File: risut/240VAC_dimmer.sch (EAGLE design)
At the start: 11 parts, among them T1 TICP206

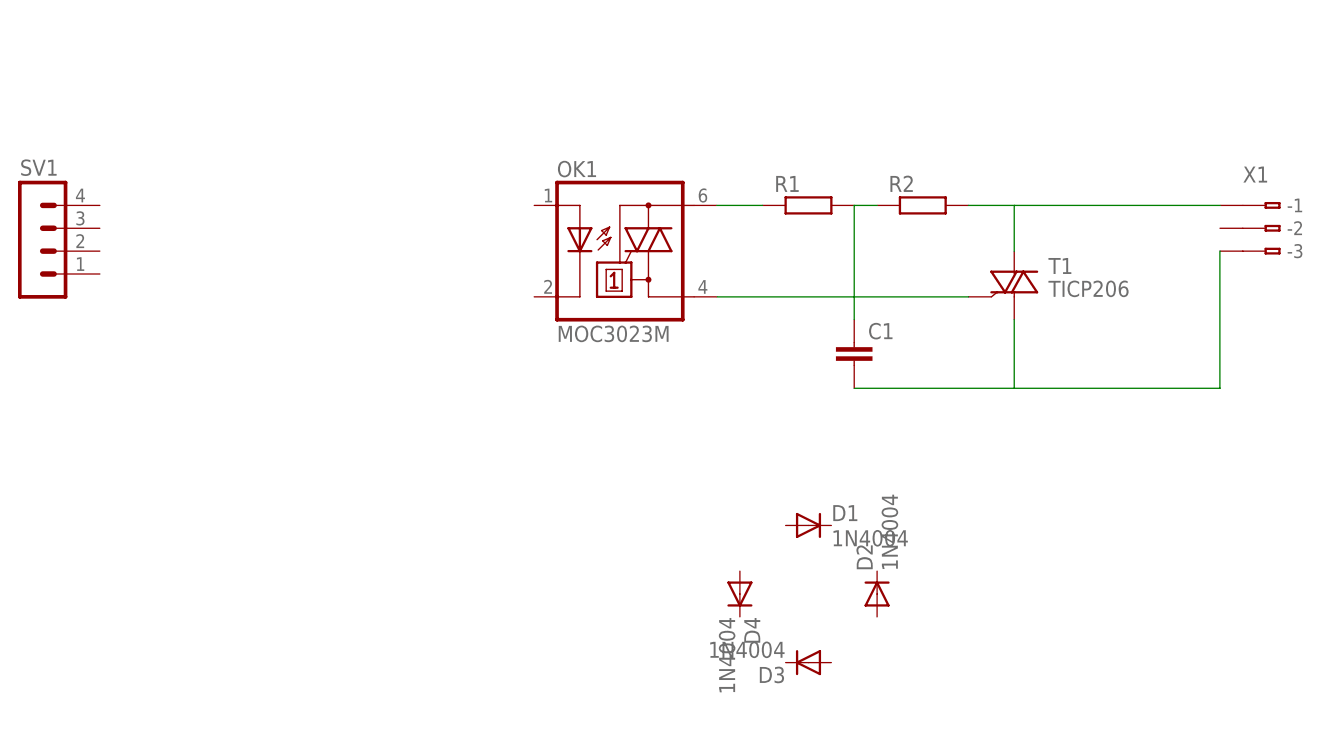
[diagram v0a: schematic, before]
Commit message: schematic of the dimmer is nearly ready
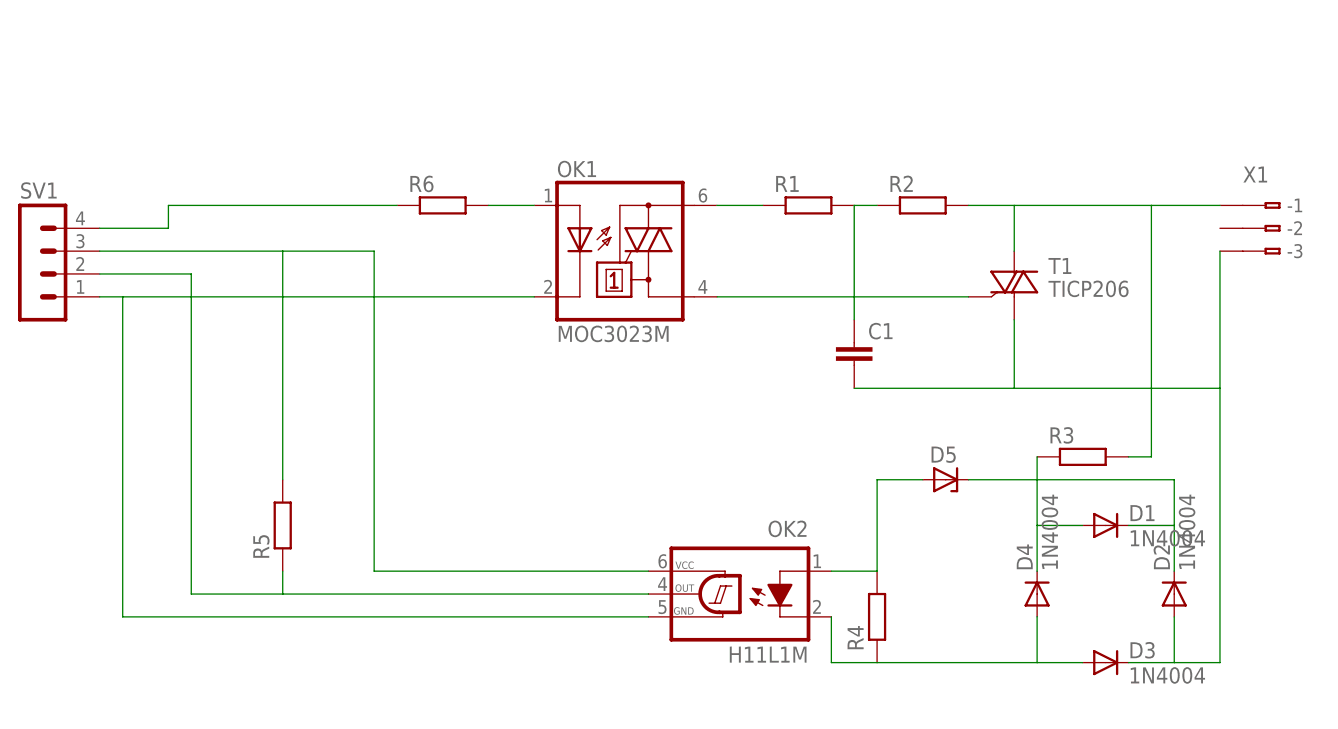
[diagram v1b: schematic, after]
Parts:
- added D5: (no value), diode:ZENER-DIODEDO41Z10
- added OK2: H11L1M, optocoupler:H11L1M
- added R3: (no value), resistor:R-EU_0207/10
- added R4, R5, R6: (no value), resistor:R-EU_0204/7
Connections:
- new net N$10: OK1.C, OK2.GND, SV1.1
- new net N$11: OK2.OUT, R5.1, SV1.2
- new net N$12: OK2.VCC, R5.2, SV1.3
- new net N$13: OK1.A, R6.2
- new net N$14: R6.1, SV1.4
- new net N$6: D1.A, D4.C, R3.1
- new net N$7: D3.A, D4.A, OK2.C, R4.1
- new net N$8: D5.A, OK2.A, R4.2
- new net N$9: D1.C, D2.C, D5.C
- net N$3: now also R3.2
- net N$5: now also D2.A, D3.C
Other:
- moved on the sheet: D1, D2, D3, D4, SV1
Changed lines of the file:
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@@
 <part name="D3" library="diode" deviceset="1N4004" device=""/>
 <part name="D4" library="diode" deviceset="1N4004" device=""/>
+<part name="R3" library="resistor" deviceset="R-EU_" device="0207/10"/>
+<part name="OK2" library="optocoupler" deviceset="H11L*M" device="" technology="1"/>
+<part name="R4" library="resistor" deviceset="R-EU_" device="0204/7"/>
+<part name="D5" library="diode" deviceset="ZENER-DIODE" device="DO41Z10"/>
+<part name="R5" library="resistor" deviceset="R-EU_" device="0204/7"/>
+<part name="R6" library="resistor" deviceset="R-EU_" device="0204/7"/>
 </parts>
 <sheets>
@@
 <instances>
 <instance part="OK1" gate="-1" x="53.34" y="68.58"/>
-<instance part="SV1" gate="1" x="-12.7" y="71.12"/>
+<instance part="SV1" gate="1" x="-12.7" y="68.58"/>
 <instance part="X1" gate="G$1" x="127" y="71.12"/>
 <instance part="T1" gate="1" x="96.52" y="63.5"/>
@@
 <instance part="R2" gate="G$1" x="86.36" y="73.66"/>
 <instance part="C1" gate="G$1" x="78.74" y="58.42"/>
-<instance part="D1" gate="1" x="73.66" y="38.1"/>
-<instance part="D2" gate="1" x="81.28" y="30.48" rot="R90"/>
-<instance part="D3" gate="1" x="73.66" y="22.86" rot="R180"/>
-<instance part="D4" gate="1" x="66.04" y="30.48" rot="R270"/>
+<instance part="D1" gate="1" x="106.68" y="38.1"/>
+<instance part="D2" gate="1" x="114.3" y="30.48" rot="R90"/>
+<instance part="D3" gate="1" x="106.68" y="22.86"/>
+<instance part="D4" gate="1" x="99.06" y="30.48" rot="R90"/>
+<instance part="R3" gate="G$1" x="104.14" y="45.72"/>
+<instance part="OK2" gate="G$1" x="66.04" y="30.48" rot="MR0"/>
+<instance part="R4" gate="G$1" x="81.28" y="27.94" rot="R90"/>
+<instance part="D5" gate="G$1" x="88.9" y="43.18"/>
+<instance part="R5" gate="G$1" x="15.24" y="38.1" rot="R90"/>
+<instance part="R6" gate="G$1" x="33.02" y="73.66"/>
 </instances>
 <busses>
@@
 </segment>
 </net>
-<net name="N$3" class="0">
-<segment>
-<pinref part="R2" gate="G$1" pin="2"/>
-<pinref part="X1" gate="G$1" pin="B-1"/>
-<wire x1="91.44" y1="73.66" x2="96.52" y2="73.66" width="0.1524" layer="91"/>
-<pinref part="T1" gate="1" pin="A2"/>
-<wire x1="96.52" y1="73.66" x2="119.38" y2="73.66" width="0.1524" layer="91"/>
-<wire x1="96.52" y1="68.58" x2="96.52" y2="73.66" width="0.1524" layer="91"/>
-</segment>
-</net>
 <net name="N$4" class="0">
 <segment>
@@
 </segment>
 </net>
+<net name="N$9" class="0">
+<segment>
+<pinref part="D1" gate="1" pin="C"/>
+<wire x1="109.22" y1="38.1" x2="114.3" y2="38.1" width="0.1524" layer="91"/>
+<pinref part="D2" gate="1" pin="C"/>
+<wire x1="114.3" y1="38.1" x2="114.3" y2="33.02" width="0.1524" layer="91"/>
+<wire x1="114.3" y1="43.18" x2="114.3" y2="38.1" width="0.1524" layer="91"/>
+<pinref part="D5" gate="G$1" pin="C"/>
+<wire x1="114.3" y1="43.18" x2="91.44" y2="43.18" width="0.1524" layer="91"/>
+</segment>
+</net>
 <net name="N$5" class="0">
 <segment>
+<pinref part="D2" gate="1" pin="A"/>
+<wire x1="114.3" y1="27.94" x2="114.3" y2="22.86" width="0.1524" layer="91"/>
 <pinref part="C1" gate="G$1" pin="2"/>
 <pinref part="X1" gate="G$1" pin="B-3"/>
@@
 <pinref part="T1" gate="1" pin="A1"/>
 <wire x1="96.52" y1="60.96" x2="96.52" y2="53.34" width="0.1524" layer="91"/>
+<wire x1="114.3" y1="22.86" x2="119.38" y2="22.86" width="0.1524" layer="91"/>
+<wire x1="119.38" y1="22.86" x2="119.38" y2="53.34" width="0.1524" layer="91"/>
+<pinref part="D3" gate="1" pin="C"/>
+<wire x1="109.22" y1="22.86" x2="114.3" y2="22.86" width="0.1524" layer="91"/>
 </segment>
 </net>
+<net name="N$3" class="0">
+<segment>
+<pinref part="R2" gate="G$1" pin="2"/>
+<pinref part="X1" gate="G$1" pin="B-1"/>
+<wire x1="91.44" y1="73.66" x2="96.52" y2="73.66" width="0.1524" layer="91"/>
+<pinref part="T1" gate="1" pin="A2"/>
+<wire x1="96.52" y1="73.66" x2="111.76" y2="73.66" width="0.1524" layer="91"/>
+<wire x1="111.76" y1="73.66" x2="119.38" y2="73.66" width="0.1524" layer="91"/>
+<wire x1="96.52" y1="68.58" x2="96.52" y2="73.66" width="0.1524" layer="91"/>
+<wire x1="111.76" y1="45.72" x2="111.76" y2="73.66" width="0.1524" layer="91"/>
+<pinref part="R3" gate="G$1" pin="2"/>
+<wire x1="109.22" y1="45.72" x2="111.76" y2="45.72" width="0.1524" layer="91"/>
+</segment>
+</net>
+<net name="N$6" class="0">
+<segment>
+<pinref part="D1" gate="1" pin="A"/>
+<wire x1="99.06" y1="38.1" x2="104.14" y2="38.1" width="0.1524" layer="91"/>
+<pinref part="R3" gate="G$1" pin="1"/>
+<wire x1="99.06" y1="38.1" x2="99.06" y2="45.72" width="0.1524" layer="91"/>
+<pinref part="D4" gate="1" pin="C"/>
+<wire x1="99.06" y1="33.02" x2="99.06" y2="38.1" width="0.1524" layer="91"/>
+</segment>
+</net>
+<net name="N$7" class="0">
+<segment>
+<pinref part="D3" gate="1" pin="A"/>
+<wire x1="104.14" y1="22.86" x2="99.06" y2="22.86" width="0.1524" layer="91"/>
+<pinref part="D4" gate="1" pin="A"/>
+<wire x1="99.06" y1="22.86" x2="99.06" y2="27.94" width="0.1524" layer="91"/>
+<pinref part="R4" gate="G$1" pin="1"/>
+<wire x1="99.06" y1="22.86" x2="81.28" y2="22.86" width="0.1524" layer="91"/>
+<wire x1="81.28" y1="22.86" x2="76.2" y2="22.86" width="0.1524" layer="91"/>
+<pinref part="OK2" gate="G$1" pin="C"/>
+<wire x1="76.2" y1="22.86" x2="76.2" y2="27.94" width="0.1524" layer="91"/>
+</segment>
+</net>
+<net name="N$8" class="0">
+<segment>
+<pinref part="R4" gate="G$1" pin="2"/>
+<pinref part="OK2" gate="G$1" pin="A"/>
+<wire x1="76.2" y1="33.02" x2="81.28" y2="33.02" width="0.1524" layer="91"/>
+<wire x1="81.28" y1="33.02" x2="81.28" y2="43.18" width="0.1524" layer="91"/>
+<pinref part="D5" gate="G$1" pin="A"/>
+<wire x1="86.36" y1="43.18" x2="81.28" y2="43.18" width="0.1524" layer="91"/>
+</segment>
+</net>
+<net name="N$10" class="0">
+<segment>
+<pinref part="OK1" gate="-1" pin="C"/>
+<pinref part="SV1" gate="1" pin="1"/>
+<wire x1="43.18" y1="63.5" x2="-2.54" y2="63.5" width="0.1524" layer="91"/>
+<pinref part="OK2" gate="G$1" pin="GND"/>
+<wire x1="-2.54" y1="63.5" x2="-5.08" y2="63.5" width="0.1524" layer="91"/>
+<wire x1="55.88" y1="27.94" x2="-2.54" y2="27.94" width="0.1524" layer="91"/>
+<wire x1="-2.54" y1="27.94" x2="-2.54" y2="63.5" width="0.1524" layer="91"/>
+</segment>
+</net>
+<net name="N$11" class="0">
+<segment>
+<pinref part="OK2" gate="G$1" pin="OUT"/>
+<wire x1="55.88" y1="30.48" x2="15.24" y2="30.48" width="0.1524" layer="91"/>
+<wire x1="15.24" y1="30.48" x2="5.08" y2="30.48" width="0.1524" layer="91"/>
+<wire x1="5.08" y1="30.48" x2="5.08" y2="66.04" width="0.1524" layer="91"/>
+<pinref part="SV1" gate="1" pin="2"/>
+<wire x1="5.08" y1="66.04" x2="-5.08" y2="66.04" width="0.1524" layer="91"/>
+<pinref part="R5" gate="G$1" pin="1"/>
+<wire x1="15.24" y1="33.02" x2="15.24" y2="30.48" width="0.1524" layer="91"/>
+</segment>
+</net>
+<net name="N$12" class="0">
+<segment>
+<pinref part="OK2" gate="G$1" pin="VCC"/>
+<wire x1="55.88" y1="33.02" x2="25.4" y2="33.02" width="0.1524" layer="91"/>
+<wire x1="25.4" y1="33.02" x2="25.4" y2="68.58" width="0.1524" layer="91"/>
+<pinref part="SV1" gate="1" pin="3"/>
+<wire x1="25.4" y1="68.58" x2="15.24" y2="68.58" width="0.1524" layer="91"/>
+<pinref part="R5" gate="G$1" pin="2"/>
+<wire x1="15.24" y1="68.58" x2="-5.08" y2="68.58" width="0.1524" layer="91"/>
+<wire x1="15.24" y1="43.18" x2="15.24" y2="68.58" width="0.1524" layer="91"/>
+</segment>
+</net>
+<net name="N$13" class="0">
+<segment>
+<pinref part="OK1" gate="-1" pin="A"/>
+<pinref part="R6" gate="G$1" pin="2"/>
+<wire x1="43.18" y1="73.66" x2="38.1" y2="73.66" width="0.1524" layer="91"/>
+</segment>
+</net>
+<net name="N$14" class="0">
+<segment>
+<pinref part="R6" gate="G$1" pin="1"/>
+<wire x1="27.94" y1="73.66" x2="2.54" y2="73.66" width="0.1524" layer="91"/>
+<wire x1="2.54" y1="73.66" x2="2.54" y2="71.12" width="0.1524" layer="91"/>
+<pinref part="SV1" gate="1" pin="4"/>
+<wire x1="2.54" y1="71.12" x2="-5.08" y2="71.12" width="0.1524" layer="91"/>
+</segment>
+</net>

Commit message: fixed a bug, added comments
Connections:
- new net N$15: R3.2, X1.B-2
- net N$3: no longer R3.2
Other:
- note added: "X1 pins: 1: L output 2: L input 3: N"
- moved on the sheet: OK2
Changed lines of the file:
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@@
 <sheet>
 <plain>
+<text x="111.76" y="81.28" size="1.778" layer="91">X1 pins:
+1:  L output
+2:  L input
+3:  N</text>
 </plain>
 <instances>
@@
 <instance part="D4" gate="1" x="99.06" y="30.48" rot="R90"/>
 <instance part="R3" gate="G$1" x="104.14" y="45.72"/>
-<instance part="OK2" gate="G$1" x="66.04" y="30.48" rot="MR0"/>
+<instance part="OK2" gate="G$1" x="50.8" y="30.48" rot="MR0"/>
 <instance part="R4" gate="G$1" x="81.28" y="27.94" rot="R90"/>
 <instance part="D5" gate="G$1" x="88.9" y="43.18"/>
@@
 <wire x1="91.44" y1="73.66" x2="96.52" y2="73.66" width="0.1524" layer="91"/>
 <pinref part="T1" gate="1" pin="A2"/>
-<wire x1="96.52" y1="73.66" x2="111.76" y2="73.66" width="0.1524" layer="91"/>
-<wire x1="111.76" y1="73.66" x2="119.38" y2="73.66" width="0.1524" layer="91"/>
+<wire x1="96.52" y1="73.66" x2="119.38" y2="73.66" width="0.1524" layer="91"/>
 <wire x1="96.52" y1="68.58" x2="96.52" y2="73.66" width="0.1524" layer="91"/>
-<wire x1="111.76" y1="45.72" x2="111.76" y2="73.66" width="0.1524" layer="91"/>
-<pinref part="R3" gate="G$1" pin="2"/>
-<wire x1="109.22" y1="45.72" x2="111.76" y2="45.72" width="0.1524" layer="91"/>
 </segment>
 </net>
@@
 <wire x1="81.28" y1="22.86" x2="76.2" y2="22.86" width="0.1524" layer="91"/>
 <pinref part="OK2" gate="G$1" pin="C"/>
-<wire x1="76.2" y1="22.86" x2="76.2" y2="27.94" width="0.1524" layer="91"/>
+<wire x1="76.2" y1="22.86" x2="60.96" y2="27.94" width="0.1524" layer="91"/>
 </segment>
 </net>
@@
 <pinref part="R4" gate="G$1" pin="2"/>
 <pinref part="OK2" gate="G$1" pin="A"/>
-<wire x1="76.2" y1="33.02" x2="81.28" y2="33.02" width="0.1524" layer="91"/>
+<wire x1="60.96" y1="33.02" x2="81.28" y2="33.02" width="0.1524" layer="91"/>
 <wire x1="81.28" y1="33.02" x2="81.28" y2="43.18" width="0.1524" layer="91"/>
 <pinref part="D5" gate="G$1" pin="A"/>
@@
 <pinref part="OK2" gate="G$1" pin="GND"/>
 <wire x1="-2.54" y1="63.5" x2="-5.08" y2="63.5" width="0.1524" layer="91"/>
-<wire x1="55.88" y1="27.94" x2="-2.54" y2="27.94" width="0.1524" layer="91"/>
+<wire x1="40.64" y1="27.94" x2="-2.54" y2="27.94" width="0.1524" layer="91"/>
 <wire x1="-2.54" y1="27.94" x2="-2.54" y2="63.5" width="0.1524" layer="91"/>
 </segment>
@@
 <segment>
 <pinref part="OK2" gate="G$1" pin="OUT"/>
-<wire x1="55.88" y1="30.48" x2="15.24" y2="30.48" width="0.1524" layer="91"/>
+<wire x1="40.64" y1="30.48" x2="15.24" y2="30.48" width="0.1524" layer="91"/>
 <wire x1="15.24" y1="30.48" x2="5.08" y2="30.48" width="0.1524" layer="91"/>
 <wire x1="5.08" y1="30.48" x2="5.08" y2="66.04" width="0.1524" layer="91"/>
@@
 <segment>
 <pinref part="OK2" gate="G$1" pin="VCC"/>
-<wire x1="55.88" y1="33.02" x2="25.4" y2="33.02" width="0.1524" layer="91"/>
+<wire x1="40.64" y1="33.02" x2="25.4" y2="33.02" width="0.1524" layer="91"/>
 <wire x1="25.4" y1="33.02" x2="25.4" y2="68.58" width="0.1524" layer="91"/>
 <pinref part="SV1" gate="1" pin="3"/>
@@
 </segment>
 </net>
+<net name="N$15" class="0">
+<segment>
+<pinref part="R3" gate="G$1" pin="2"/>
+<wire x1="109.22" y1="45.72" x2="111.76" y2="45.72" width="0.1524" layer="91"/>
+<wire x1="111.76" y1="45.72" x2="111.76" y2="71.12" width="0.1524" layer="91"/>
+<pinref part="X1" gate="G$1" pin="B-2"/>
+<wire x1="111.76" y1="71.12" x2="119.38" y2="71.12" width="0.1524" layer="91"/>
+</segment>
+</net>
 </nets>
 </sheet>
@@
 </schematic>
 </drawing>
+<compatibility>
+<note version="6.3" minversion="6.2.2" severity="warning">
+Since Version 6.2.2 text objects can contain more than one line,
+which will not be processed correctly with this version.
+</note>
+</compatibility>
 </eagle>

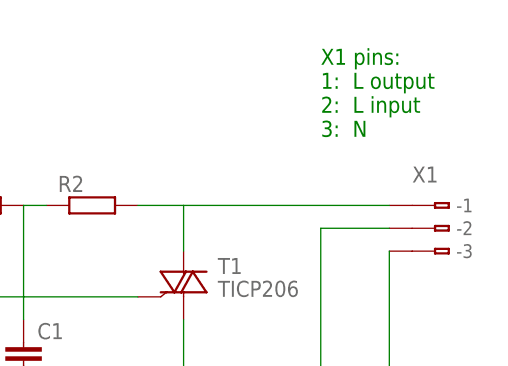
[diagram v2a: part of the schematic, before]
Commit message: fixed a bug in dimmer: X1 pin configuration was wrong
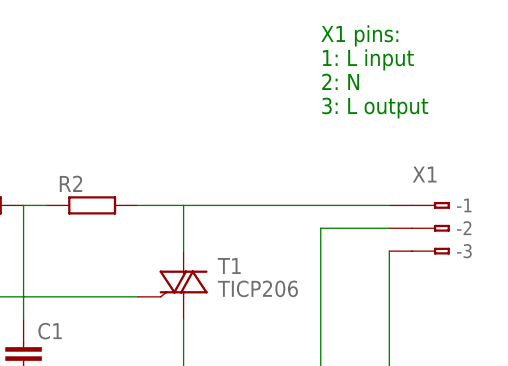
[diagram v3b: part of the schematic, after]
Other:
- note added: "X1 pins: 1: L input 2: N 3: L output"
- note removed: "X1 pins: 1: L output 2: L input 3: N"
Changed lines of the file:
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@@
 <sheet>
 <plain>
-<text x="111.76" y="81.28" size="1.778" layer="91">X1 pins:
-1:  L output
-2:  L input
-3:  N</text>
+<text x="111.76" y="83.82" size="1.778" layer="91">X1 pins:
+1: L input
+2: N
+3: L output</text>
 </plain>
 <instances>
